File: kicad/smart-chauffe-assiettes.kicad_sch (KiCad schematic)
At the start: 16 parts, among them J1 Conn_01x08_Socket, U1 PIC10F202-IP

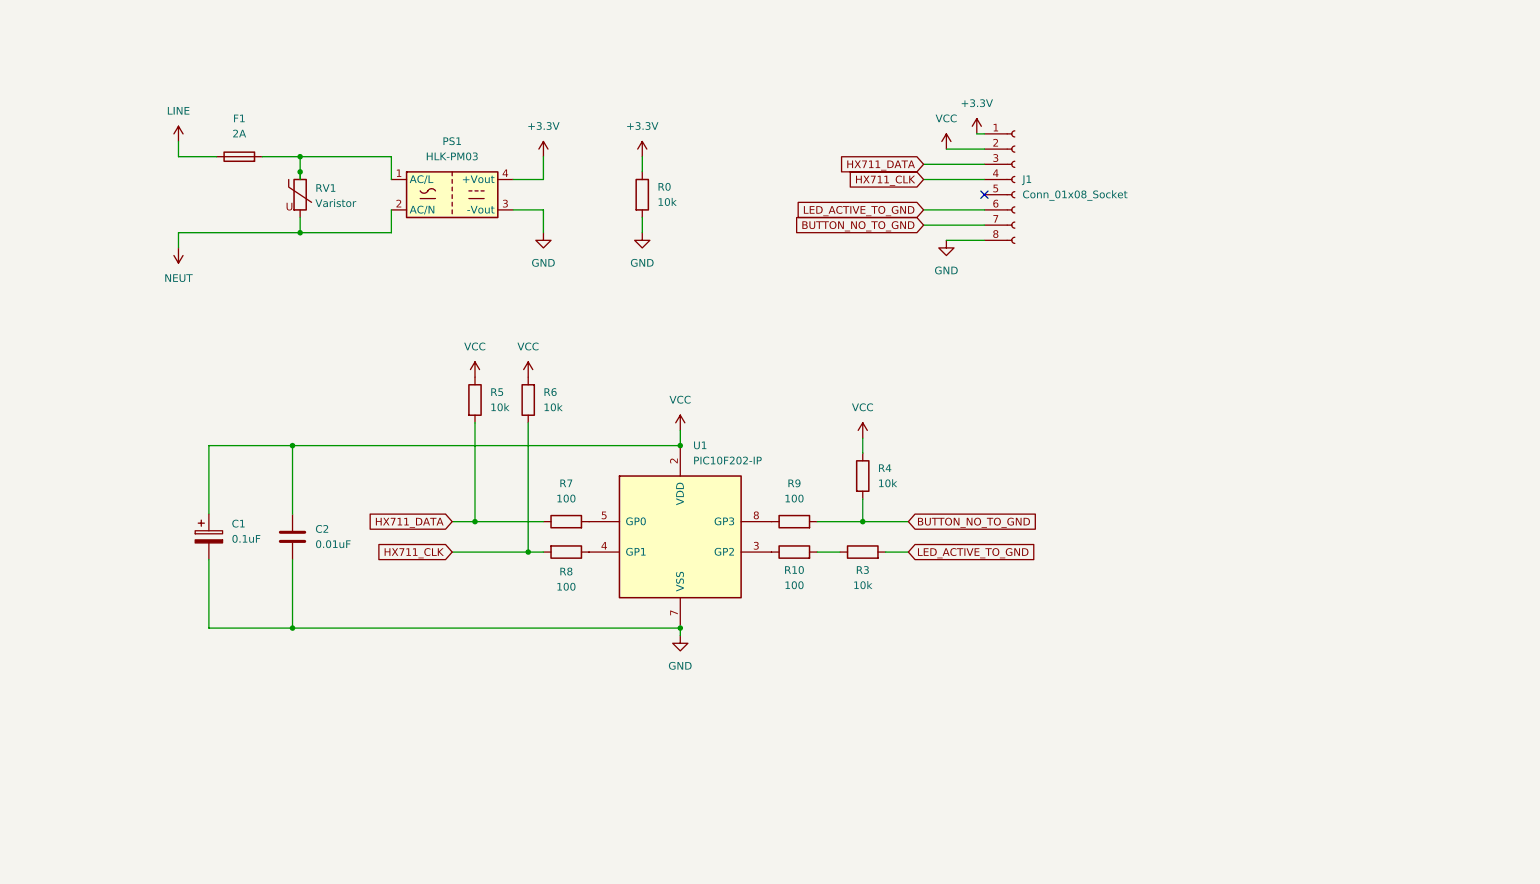
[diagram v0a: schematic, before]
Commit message: Finalize schematic : inverted relay and sop23-to-dip6 adapter
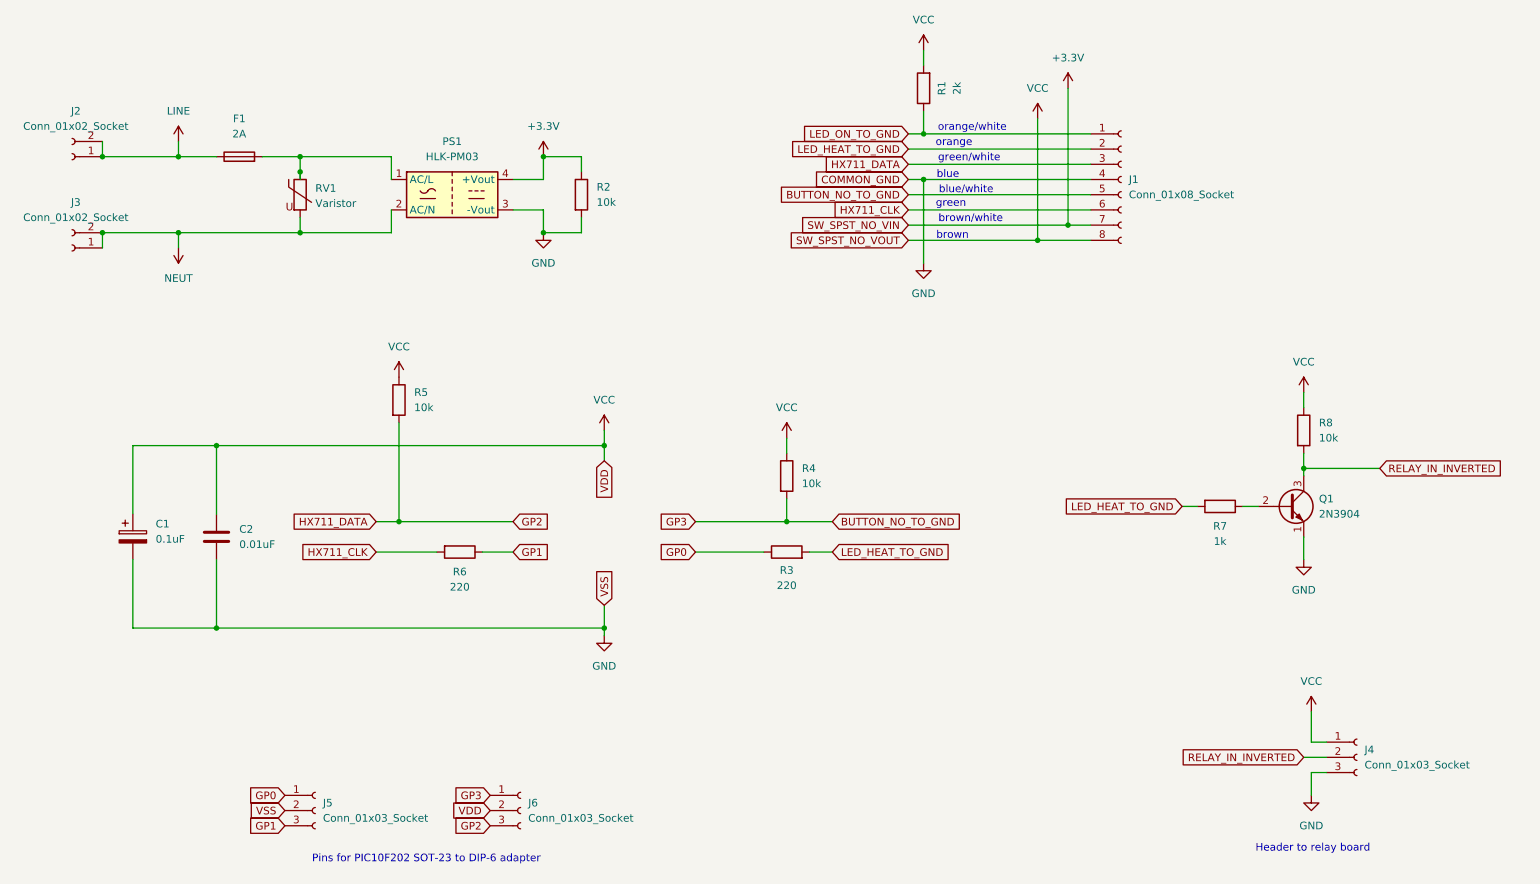
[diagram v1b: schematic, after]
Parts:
- removed R10, R9: 100, Resistor_THT:R_Axial_DIN0207_L6.3mm_D2.5mm_P2.54mm_Vertical, symbol Device:R
- removed R6: 10k, Resistor_THT:R_Axial_DIN0207_L6.3mm_D2.5mm_P2.54mm_Vertical, symbol Device:R
- removed U1: PIC10F202-IP, Package_DIP:DIP-8_W7.62mm, symbol MCU_Microchip_PIC10:PIC10F202-IP
- added J2, J3: Conn_01x02_Socket, TerminalBlock_Phoenix:TerminalBlock_Phoenix_MKDS-1,5-2-5.08_1x02_P5.08mm_Horizontal, symbol Connector:Conn_01x02_Socket
- added J4: Conn_01x03_Socket, symbol Connector:Conn_01x03_Socket
- added J5, J6: Conn_01x03_Socket, Connector_PinSocket_2.54mm:PinSocket_1x03_P2.54mm_Vertical, symbol Connector:Conn_01x03_Socket
- added Q1: 2N3904, Package_TO_SOT_THT:TO-92_Inline_Wide, symbol Transistor_BJT:2N3904
- added R1: 2k, Resistor_THT:R_Axial_DIN0207_L6.3mm_D2.5mm_P2.54mm_Vertical, symbol Device:R
- added R8: 10k, Resistor_THT:R_Axial_DIN0207_L6.3mm_D2.5mm_P2.54mm_Vertical, symbol Device:R
- R3: value 10k -> 220
- R6: renamed from R8; value 100 -> 220
- R7: value 100 -> 1k
- renumbered R0 to R2
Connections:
- net +3.3V: now also J1.7 (Pin_7); no longer J1.1 (Pin_1)
- net BUTTON_NO_TO_GND: now also J1.5 (Pin_5), J6.1 (Pin_1); no longer J1.7 (Pin_7)
- net GND: now also J1.4 (Pin_4), J4.3 (Pin_3), J5.2 (Pin_2), Q1.1 (E); no longer J1.8 (Pin_8)
- net HX711_CLK: now also J1.6 (Pin_6); no longer J1.4 (Pin_4)
- net LINE: now also J2.1 (Pin_1), J2.2 (Pin_2)
- net NEUT: now also J3.1 (Pin_1), J3.2 (Pin_2)
- net VCC: now also J1.8 (Pin_8), J4.1 (Pin_1), J6.2 (Pin_2), R1.2, R8.1; no longer J1.2 (Pin_2)
- net LED_HEAT_TO_GND: now reaches R7.2
- net LED_HEAT_TO_GND: now also J1.2 (Pin_2), R3.2
- net GP1: now reaches R6.1
- net GP1: now also J5.3 (Pin_3)
- net GP0: now reaches R3.1
- net GP0: now also J5.1 (Pin_1)
- net HX711_DATA renamed GP2
- net GP2: now also J6.3 (Pin_3); no longer R7.1
- removed net LED_ACTIVE_TO_GND: J1.6 (Pin_6), R3.2
- new net: Q1.2 (B), R7.1
- new net LED_ON_TO_GND: J1.1 (Pin_1), R1.1
- new net RELAY_IN_INVERTED: J4.2 (Pin_2), Q1.3 (C), R8.2
- no-connect marks 1 -> 0
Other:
- note added: "Header to relay board"
- note added: "Pins for PIC10F202 SOT-23 to DIP-6 adapter"
- note added: "blue"
- note added: "blue/white"
- note added: "brown"
- note added: "brown/white"
- note added: "green"
- note added: "green/white"
- note added: "orange"
- note added: "orange/white"
- moved on the sheet: C1, C2, J1, R2, R3, R4, R5, R6

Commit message: Fix footprint for header to relay input
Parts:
- J4: footprint (none) -> TerminalBlock_Phoenix:TerminalBlock_Phoenix_MKDS-1,5-3-5.08_1x03_P5.08mm_Horizontal
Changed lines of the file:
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@@
 			)
 		)
-		(property "Footprint" ""
+		(property "Footprint" "TerminalBlock_Phoenix:TerminalBlock_Phoenix_MKDS-1,5-3-5.08_1x03_P5.08mm_Horizontal"
 			(at 238.76 142.24 0)
 			(effects

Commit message: Add text for design info and rename power networks
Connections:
- net FUSED: now reaches F1.2, PS1.1 (AC/L), RV1.1
- net LINE renamed PHASE
- net NEUT renamed NEUTRAL
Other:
- note added: "Drain resistor"
- note added: "Handle disconnect"
- note added: "Header to relay board input"
- note added: "Less current for green led"
- note added: "More current for yellow led"
- note added: "Pins for PIC10F202 SOT-23 to DIP-6 adapter ... because i bought SOP23 but solder on perfboards !"
- note added: "Short protection (max 15mA)"
- note added: "This could have been avoided if i wired LEAD_HEAT led from VCC instead of to ground... in hindsight !"
- note removed: "Header to relay board"
- note removed: "Pins for PIC10F202 SOT-23 to DIP-6 adapter"
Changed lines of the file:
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@@
 		)
 	)
+	(text "Less current for green led"
+		(exclude_from_sim no)
+		(at 150.876 30.48 0)
+		(effects
+			(font
+				(size 1.27 1.27)
+			)
+		)
+	)
+	(text "Short protection (max 15mA)"
+		(exclude_from_sim no)
+		(at 90.17 116.84 0)
+		(effects
+			(font
+				(size 1.27 1.27)
+			)
+		)
+	)
 	(text "blue"
 		(exclude_from_sim no)
@@
 		)
 	)
-	(text "Pins for PIC10F202 SOT-23 to DIP-6 adapter"
+	(text "Drain\nresistor"
+		(exclude_from_sim no)
+		(at 120.396 48.26 0)
+		(effects
+			(font
+				(size 1.27 1.27)
+			)
+		)
+	)
+	(text "More current for yellow led"
+		(exclude_from_sim no)
+		(at 161.798 113.284 0)
+		(effects
+			(font
+				(size 1.27 1.27)
+			)
+		)
+	)
+	(text "Handle disconnect"
+		(exclude_from_sim no)
+		(at 67.564 82.55 0)
+		(effects
+			(font
+				(size 1.27 1.27)
+			)
+		)
+	)
+	(text "Pins for PIC10F202 SOT-23 to DIP-6 adapter ...\nbecause i bought SOP23 but solder on perfboards !"
 		(exclude_from_sim no)
 		(at 83.312 159.258 0)
@@
 		)
 	)
-	(text "Header to relay board"
+	(text "Header to relay board input"
 		(exclude_from_sim no)
 		(at 231.394 157.48 0)
@@
 		)
 	)
+	(text "Handle disconnect"
+		(exclude_from_sim no)
+		(at 159.258 95.504 0)
+		(effects
+			(font
+				(size 1.27 1.27)
+			)
+		)
+	)
 	(text "green/white"
 		(exclude_from_sim no)
@@
 		)
 	)
+	(text "This could have been avoided if i wired LEAD_HEAT\nled from VCC instead of to ground... in hindsight !"
+		(exclude_from_sim no)
+		(at 225.298 70.866 0)
+		(effects
+			(font
+				(size 1.27 1.27)
+			)
+		)
+	)
 	(text "blue/white"
 		(exclude_from_sim no)
@@
 	(wire
 		(pts
+			(xy 62.23 39.37) (xy 62.23 41.91)
+		)
+		(stroke
+			(width 0)
+			(type default)
+		)
+	)
+	(wire
+		(pts
 			(xy 166.37 38.1) (xy 194.31 38.1)
 		)
@@
 	)
 	(symbol
+		(lib_id "power:LINE")
+		(at 62.23 39.37 0)
+		(unit 1)
+		(exclude_from_sim no)
+		(in_bom yes)
+		(on_board yes)
+		(dnp no)
+		(fields_autoplaced yes)
+		(property "Reference" "#PWR013"
+			(at 62.23 43.18 0)
+			(effects
+				(font
+					(size 1.27 1.27)
+				)
+				(hide yes)
+			)
+		)
+		(property "Value" "FUSED"
+			(at 62.23 34.29 0)
+			(effects
+				(font
+					(size 1.27 1.27)
+				)
+			)
+		)
+		(property "Footprint" ""
+			(at 62.23 39.37 0)
+			(effects
+				(font
+					(size 1.27 1.27)
+				)
+				(hide yes)
+			)
+		)
+		(property "Datasheet" ""
+			(at 62.23 39.37 0)
+			(effects
+				(font
+					(size 1.27 1.27)
+				)
+				(hide yes)
+			)
+		)
+		(property "Description" "Power symbol creates a global label with name \"LINE\""
+			(at 62.23 39.37 0)
+			(effects
+				(font
+					(size 1.27 1.27)
+				)
+				(hide yes)
+			)
+		)
+		(pin "1"
+		)
+		(instances
+			(project "smart-chauffe-assiettes"
+				(path "/ce582257-7618-43dc-a01a-d7f6978c4483"
+					(reference "#PWR013")
+					(unit 1)
+				)
+			)
+		)
+	)
+	(symbol
 		(lib_id "power:VCC")
 		(at 78.74 78.74 0)
@@
 			)
 		)
-		(property "Value" "LINE"
+		(property "Value" "PHASE"
 			(at 41.91 34.29 0)
 			(effects
@@
 			)
 		)
-		(property "Value" "NEUT"
+		(property "Value" "NEUTRAL"
 			(at 41.91 62.23 0)
 			(effects

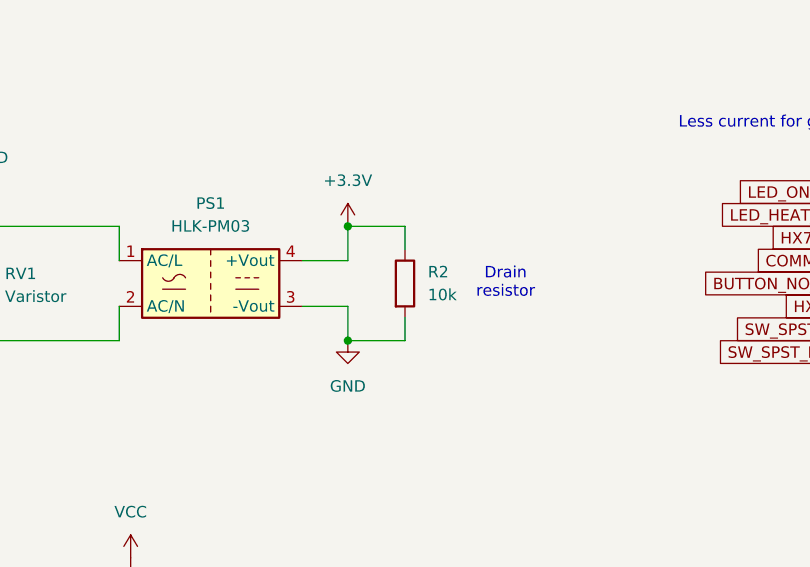
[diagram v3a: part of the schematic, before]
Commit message: Fix missing power trace and swap psu leads
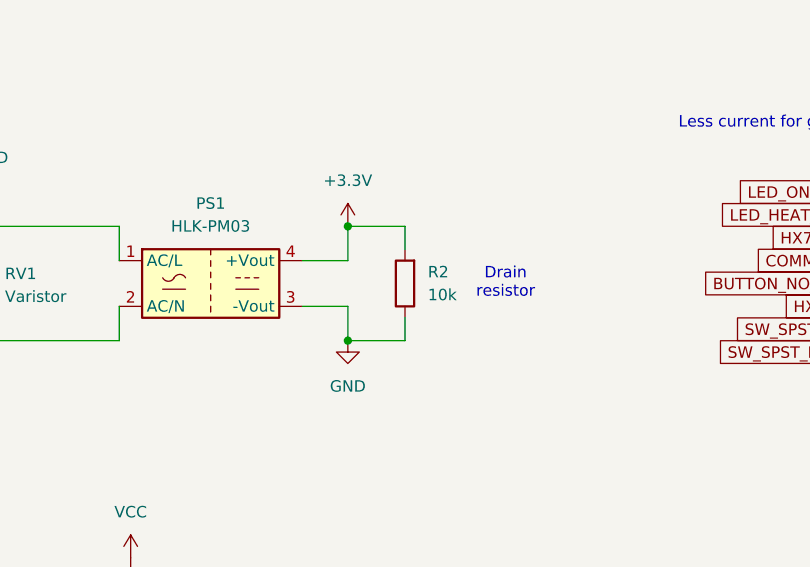
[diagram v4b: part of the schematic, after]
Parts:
- R2: footprint Resistor_THT:R_Axial_DIN0207_L6.3mm_D2.5mm_P2.54mm_Vertical -> Resistor_THT:R_Axial_DIN0207_L6.3mm_D2.5mm_P7.62mm_Horizontal
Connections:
- net +3.3V: now also R2.2; no longer R2.1
- net GND: now also R2.1; no longer R2.2
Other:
- moved on the sheet: R2
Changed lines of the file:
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@@
 	(symbol
 		(lib_id "Device:R")
-		(at 109.22 48.26 0)
+		(at 109.22 48.26 180)
 		(unit 1)
 		(exclude_from_sim no)
@@
 					(size 1.27 1.27)
 				)
-				(justify left)
+				(justify right)
 			)
 		)
@@
 					(size 1.27 1.27)
 				)
-				(justify left)
+				(justify right)
 			)
 		)
-		(property "Footprint" "Resistor_THT:R_Axial_DIN0207_L6.3mm_D2.5mm_P2.54mm_Vertical"
-			(at 107.442 48.26 90)
+		(property "Footprint" "Resistor_THT:R_Axial_DIN0207_L6.3mm_D2.5mm_P7.62mm_Horizontal"
+			(at 110.998 48.26 90)
 			(effects
 				(font
